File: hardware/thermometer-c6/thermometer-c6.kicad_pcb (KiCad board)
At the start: 2 copper layers, 49 x 36 mm, 101 parts, among them J1 JST-PH-2 BAT, J2 MEAS_HDR, J3 USB-C, J4 EPD FPC24 0.5mm, J5 DEBUG, Q1 AO3401A, Q2 AO3401A, Q3 Si1308EDL, Q4 AO3401A, Q5 2N7002, Q6 AO3401A, SW1 RESET, SW2 BOOT, U1 ESP32-C6-MINI-1-N4, U2 RT9080-33GJ5, U3 USBLC6-2SC6, U4 MCP73831-2, U5 BMP581, U6 BMP585, Y1 32.768kHz FC-135

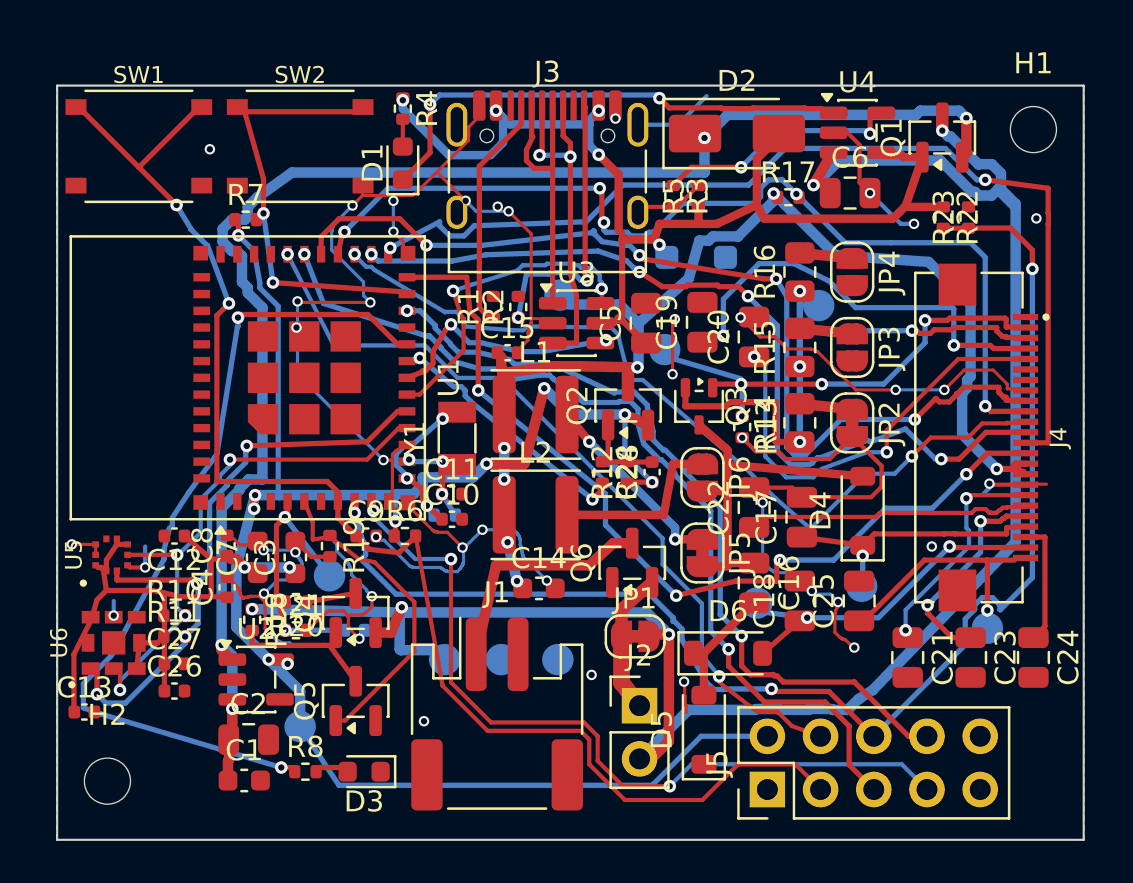
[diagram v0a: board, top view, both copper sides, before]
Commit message: Reclaim 48x35 board size; harvest user's GND re-stitch (0 unconnected)
Shrank BOARD to 48x35 (both east+south strips reclaimed to original
size). The outline shrink re-fragmented the GND pour into 3 opens
(C12.2, U3.2, an F<->B split); the user hand-closed them in the GUI.
Harvested wholesale (56 GND tracks / 44 stitch vias). Also adds
verify/gnd_islands.py -- a GND connectivity/robustness debugger
(island-aware via pcbnew GetUnconnectedCount; finds articulation vias +
recommends redundant-via spots). Gate: unconnected 0, REAL=0 (2 GND
dangling stubs deferred), check_pcb OK, make check green. Archive
snapshot of the solved board included.

Note: GND is connected but LOW-redundancy -- two sub-planes (~49/~38
pads) each hang off a single 0.15mm neck; hardening next.

Co-Authored-By: Claude Fable 5 <noreply@anthropic.com>
Claude-Session: https://claude.ai/code/session_017pkZ81qmZpNwwW2CABSh5y
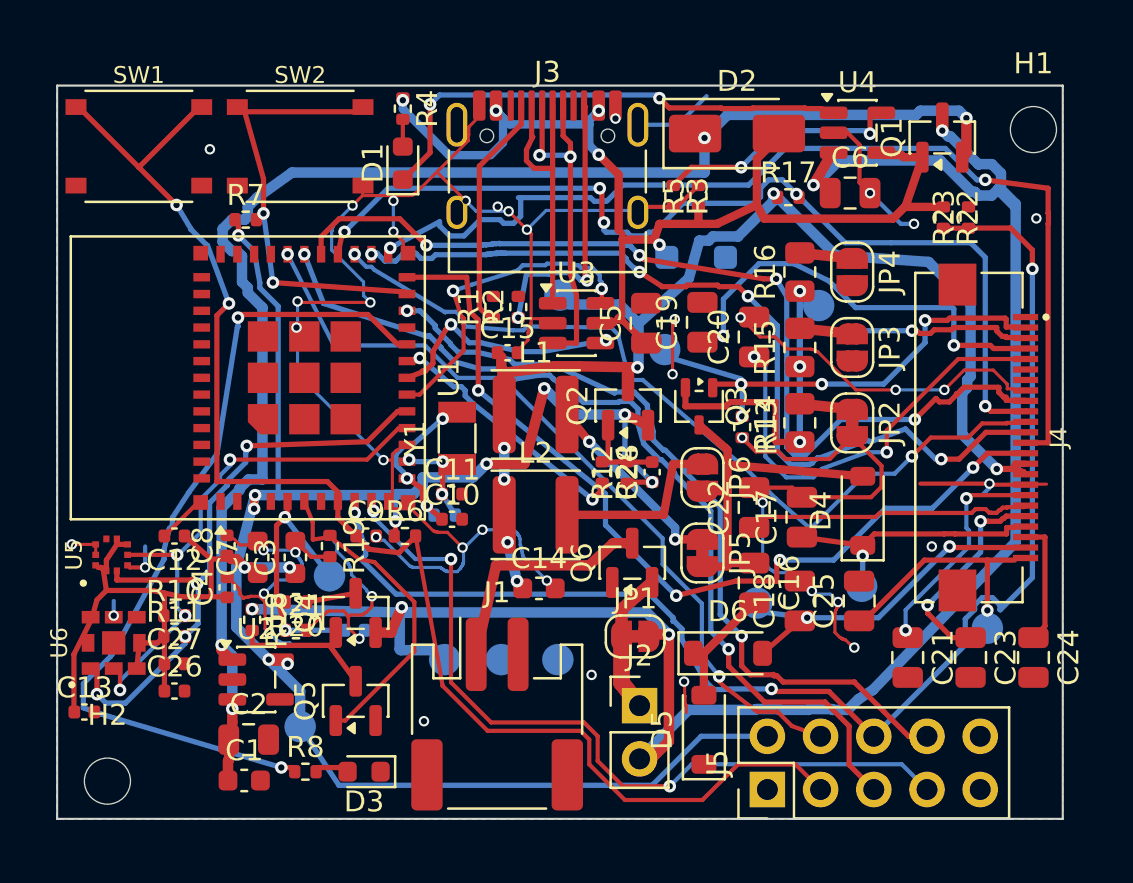
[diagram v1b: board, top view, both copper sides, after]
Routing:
- net GND: track 149.3 -> 161.5 mm, vias 43 -> 44
- net EPD_CS: track 40.5 -> 41.9 mm
- net EPD_SCK: track 47.6 -> 48.6 mm
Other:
- board size 49 x 36 mm -> 48 x 35 mm

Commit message: Harden GND: +10 redundant stitch vias, single-via SPOFs 28 -> 18
verify/gnd_islands.py audit found GND connected but a low-redundancy
tree. Added 10 GND stitch vias (0.5/0.3): 7 doubling small single-via
ties + 3 doubling the largest via-SPOFs (the 46/27-pad planes and the
user's 27-pad HV via @22.42,6.88 now has a redundant tie @23.0,6.5).
Single-via ties 28->18; the four biggest are de-SPOF'd. Gate REAL=0,
unconnected 0, check_pcb OK, make check green.

KNOWN RESIDUAL (needs a GUI reroute, not stitchable): the whole GND is
two board-spanning halves (~39 + ~61 pads) joined by ONE 0.15mm F.Cu
neck at the crystal/EN moat (TRACKS ~line 206) -- no bypass via exists
(the halves meet cross-layer only there) and widening fails DRC on the
crystal clearance. Opening a 2nd GND crossing of that moat is the top
robustness item.

Co-Authored-By: Claude Fable 5 <noreply@anthropic.com>
Claude-Session: https://claude.ai/code/session_017pkZ81qmZpNwwW2CABSh5y
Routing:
- net GND: vias 44 -> 54
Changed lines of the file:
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@@
+	)
+	(via
+		(at 100.85 122.74)
+		(size 0.5)
+		(drill 0.3)
+		(layers "F.Cu" "B.Cu")
+		(net "GND")
 	)
 	(via
@@
 	)
 	(via
+		(at 112.08 112.1)
+		(size 0.5)
+		(drill 0.3)
+		(layers "F.Cu" "B.Cu")
+		(net "GND")
+	)
+	(via
+		(at 113.3 105.43)
+		(size 0.5)
+		(drill 0.3)
+		(layers "F.Cu" "B.Cu")
+		(net "GND")
+	)
+	(via
 		(at 113.717 106.983)
 		(size 0.6)
@@
 	)
 	(via
+		(at 114.9 118.5)
+		(size 0.5)
+		(drill 0.3)
+		(layers "F.Cu" "B.Cu")
+		(net "GND")
+	)
+	(via
 		(at 114.95 110.35)
 		(size 0.5)
@@
 	)
 	(via
+		(at 117.06 105.79)
+		(size 0.5)
+		(drill 0.3)
+		(layers "F.Cu" "B.Cu")
+		(net "GND")
+	)
+	(via
 		(at 117.312 113.003)
 		(size 0.6)
@@
 	)
 	(via
+		(at 118.36 130.34)
+		(size 0.5)
+		(drill 0.3)
+		(layers "F.Cu" "B.Cu")
+		(net "GND")
+	)
+	(via
 		(at 118.37 119.5)
 		(size 0.6)
@@
 	)
 	(via
+		(at 123 106.5)
+		(size 0.5)
+		(drill 0.3)
+		(layers "F.Cu" "B.Cu")
+		(net "GND")
+	)
+	(via
 		(at 123.025 103.325)
 		(size 0.6)
@@
 	)
 	(via
+		(at 125.77 128.94)
+		(size 0.5)
+		(drill 0.3)
+		(layers "F.Cu" "B.Cu")
+		(net "GND")
+	)
+	(via
 		(at 125.85 101.2)
 		(size 0.6)
@@
 	)
 	(via
+		(at 126 123.3)
+		(size 0.5)
+		(drill 0.3)
+		(layers "F.Cu" "B.Cu")
+		(net "GND")
+	)
+	(via
 		(at 126.1 106.534)
 		(size 0.6)
@@
 	)
 	(via
+		(at 139.65 105.13)
+		(size 0.5)
+		(drill 0.3)
+		(layers "F.Cu" "B.Cu")
+		(net "GND")
+	)
+	(via

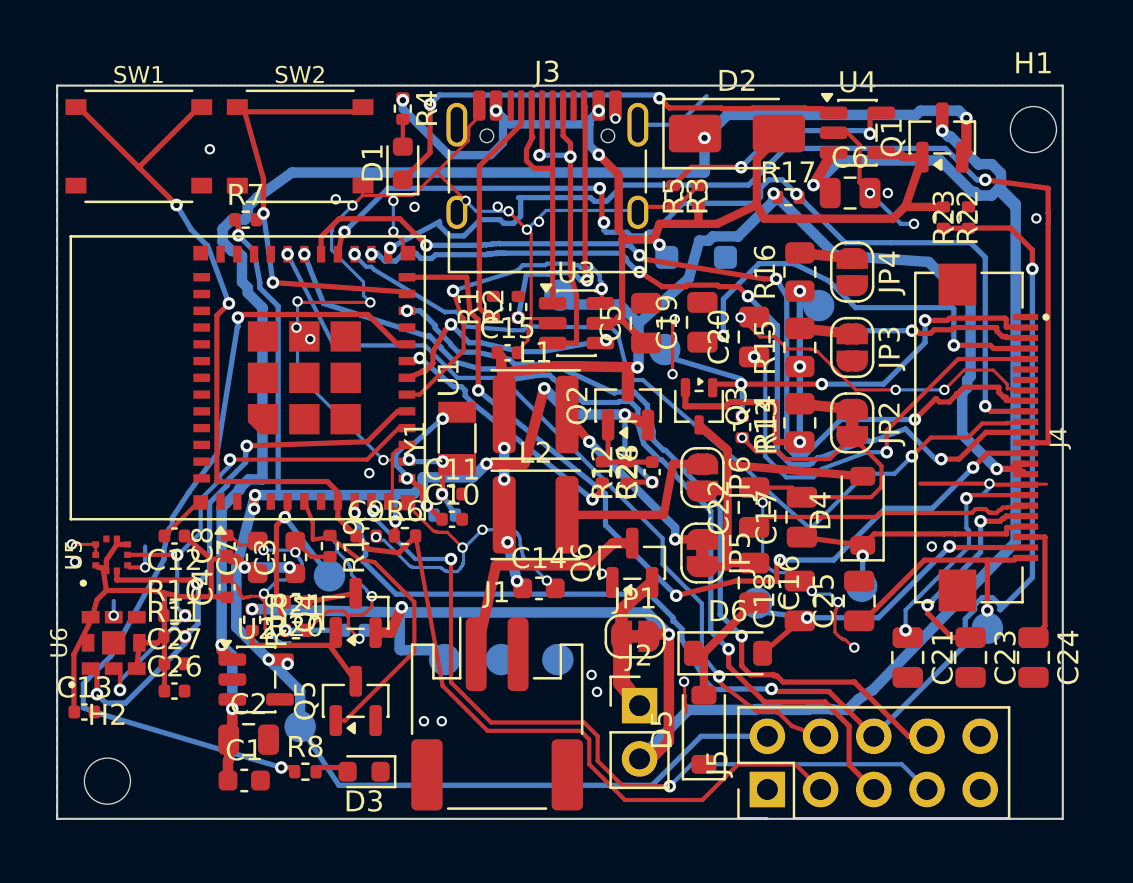
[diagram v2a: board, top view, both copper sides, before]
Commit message: Harvest GND-SPOF fixes + straighten all paths to fixpoint
Harvested the user's GND-robustness GUI pass (single-via SPOF ties
15->2, crystal/EN moat eliminated). Fixed the 2 hole_to_hole (nudged
GND stitch vias to >=0.25 hole-to-hole) + 2 dangling stubs their vias
introduced. Straightened both signal (pcb_routes) and GND (pcb_layout
TRACKS) polylines to a true fixpoint (re-run fresh until 0 accepted, 2
runs each): -138 vertices, -17.3mm copper -> more pour area.

straighten.py: added --layout (straighten pcb_layout GND TRACKS, STITCH
vias as junction guards) and FIXED a latent gate bug -- it waived
GND-unconnected, which on a finished board silently deleted a vertex on
U5.8's sensor-GND pad (under the fills=False keep-out, no pour fallback)
and disconnected it. Gate now requires unconnected==0 for all nets.

Gate REAL=0, unconnected 0, check_pcb OK, make check green, GND
connected. Archive snapshot of the user's solve included. Widen pass
next; not reviewed yet.

Co-Authored-By: Claude Fable 5 <noreply@anthropic.com>
Claude-Session: https://claude.ai/code/session_017pkZ81qmZpNwwW2CABSh5y
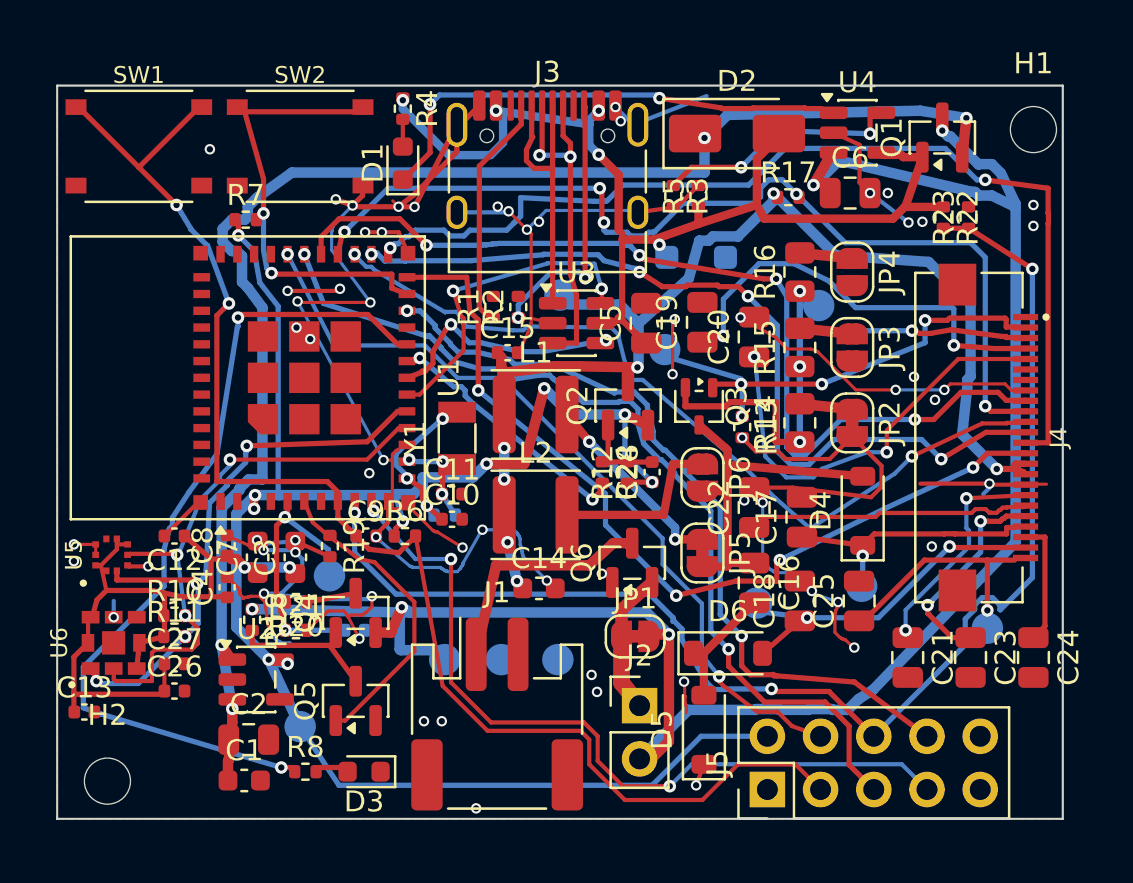
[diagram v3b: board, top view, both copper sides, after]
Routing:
- net GND: track 161.5 -> 176.6 mm, vias 54 -> 66
- net +3V3: track 112.4 -> 116.2 mm
- net SDA: track 25.6 -> 27.7 mm, vias 4 -> 3
- net EPD_CS: track 41.9 -> 40.2 mm
- net VBAT: track 91.5 -> 90.3 mm
- net SCL: track 29.9 -> 28.8 mm
- net EPD_MOSI: track 42.3 -> 41.5 mm
- net VBUS_SENSE: track 64.2 -> 63.5 mm
- net VBUS: track 53.1 -> 52.4 mm
- net EPD_DC: track 40.1 -> 39.5 mm
- net VDIV_EN: track 15.4 -> 14.8 mm
- net VSYS: track 72.2 -> 71.7 mm
- net Net-(J3-CC2): track 13.6 -> 13.1 mm

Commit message: Harvest hand-routed neck + east-cap GND SPOF fixes
North F.Cu GND neck (0.25mm, was sole tie for ~34 pads) re-laced; east-cap 16-pad SPOF given a 2nd tie via a 0.6/0.3 stitch at (44.70,6.40). Signals harvested via extract_tracks --all; GND vias -> STITCH (66->68, grown sizes preserved), lacing -> TRACKS. out/hand == generated is copper-identical (1075 segments / 191 vias, +0/-0 per net); DRC REAL=0, unconnected=0, starved=0; make check green.

Co-Authored-By: Claude Opus 4.8 (1M context) <noreply@anthropic.com>
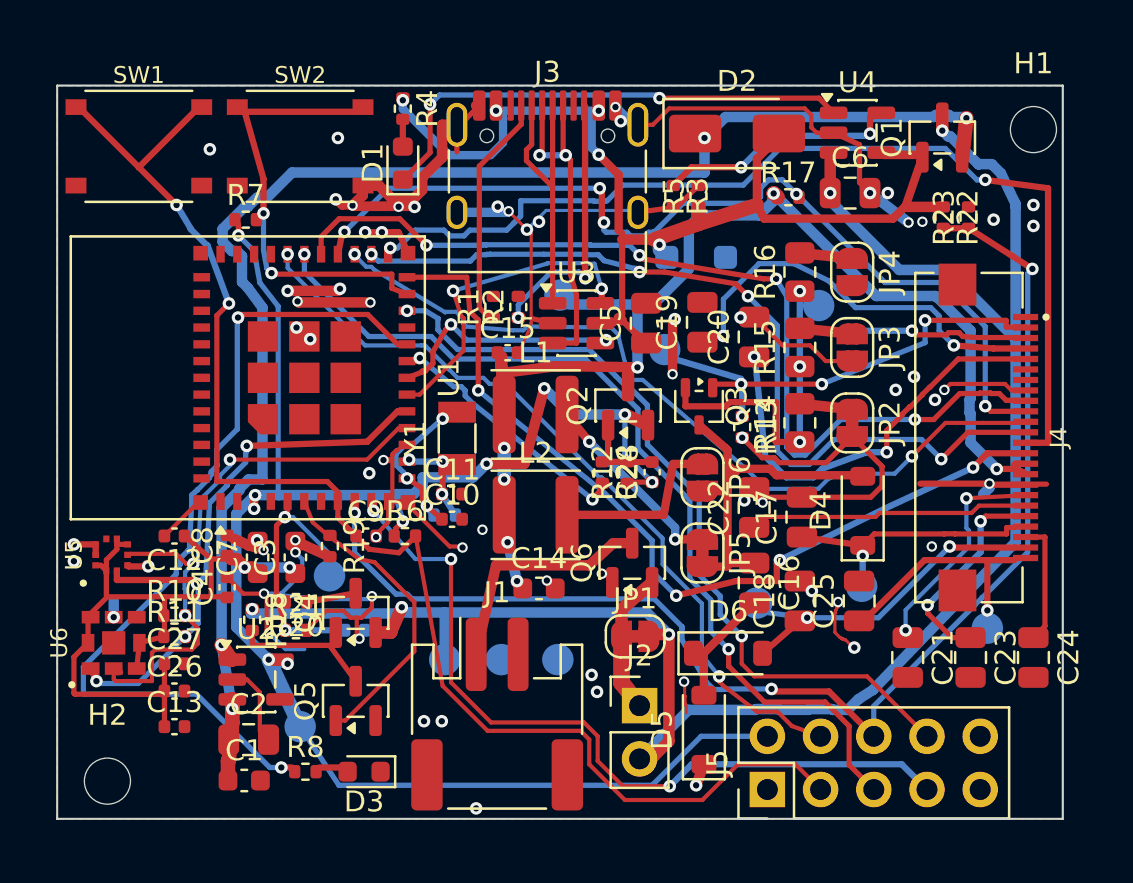
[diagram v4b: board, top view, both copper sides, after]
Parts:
- moved C12 9.44 mm to (105.6, 121.5), turned to 180 degrees
- moved C27 6.10 mm to (105.6, 127.6), turned to 0 degrees
- moved C13 1.70 mm to (105.6, 130.6)
- moved C26 1.30 mm to (105.6, 128.9)
- renumbered C13 to C12, C26 to C13, C27 to C26, C12 to C27
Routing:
- net GND: track 176.6 -> 150.6 mm, vias 66 -> 68
- net EPD_RST: track 46.8 -> 44.9 mm
- net VBUS_SENSE: track 63.5 -> 61.9 mm
- net LED_STATUS: track 40.2 -> 41.2 mm
- net DBG_IO8: track 37.4 -> 38.4 mm
- net SDA: track 27.7 -> 28.6 mm
- net +3V3: track 116.2 -> 117.0 mm
- net CHG_STAT: track 22.7 -> 23.5 mm
- net EPD_DC: track 39.5 -> 38.8 mm
- net Net-(J4-Pin_4): track 19.3 -> 18.7 mm
- net VBAT: track 90.3 -> 90.8 mm

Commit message: Straighten to fixpoint + widen traces/GND toward class caps
Straighten: signals -43 verts/-6.80mm, GND lacing -15 verts/-1.41mm (collapsed +3V3 B.Cu S-bend, DBG_RX slivers, EPD_CS/BUSY/USB_D kinks; VDIV_EN staircase is genuine corners, left). Widen: +8.1mm2 -- signals normalized toward 0.30, power/burst toward 0.70; GND neck (20.15,0.95) hardened 0.25->0.50. Converged in 2 straighten<->widen rounds. 0 vias pruned: NE double-stitch pair is mutually load-bearing, board is not over-stitched. DRC REAL=0/unconnected=0/starved=0, gnd_islands 1 island (no new SPOF), make check green, byte-stable.

Co-Authored-By: Claude Opus 4.8 (1M context) <noreply@anthropic.com>
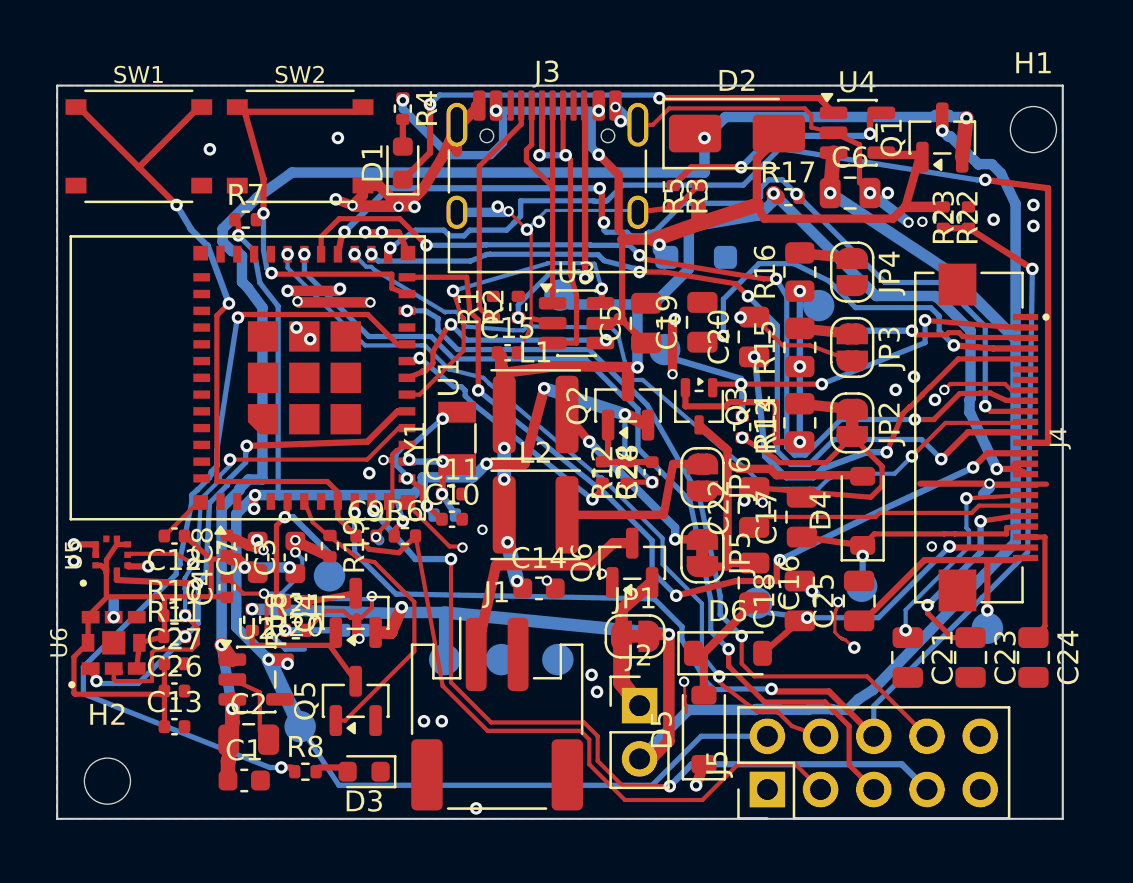
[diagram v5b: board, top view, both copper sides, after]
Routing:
- net GND: track 150.6 -> 149.2 mm
- net VBAT: track 90.8 -> 89.4 mm
- net LED_STATUS: track 41.2 -> 39.9 mm
- net DBG_IO8: track 38.4 -> 37.7 mm
- net EPD_SCK: track 48.1 -> 47.5 mm

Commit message: Harvest hand reroute pass; restore DBG_TX bridge dropped as graphic line
Large GUI simplification pass (~30 nets tidied: LED_STATUS -11, DBG_TX -10, VSYS/VBAT -8/-7, SDA/SCL -7/-5, USB_D+ -5, EPD_MOSI +4; vias unchanged). The DBG_TX gap had been bridged with a copper PCB_SHAPE graphic line, which extract_tracks (GetTracks only) drops -> reproduced as a proper netted DBG_TX track (0 unconnected, DRC-validated). Trimmed a 0.099mm EPD_DC dangling stub. Signals via extract_tracks --all; GND STITCH 68 (grown sizes preserved) + TRACKS 47. out/hand == generated (topo 59/59); DRC REAL=0, unconnected=0, starved=0; make check green; byte-stable. 27-pad B.Cu neck (#35) still open.

Co-Authored-By: Claude Opus 4.8 (1M context) <noreply@anthropic.com>
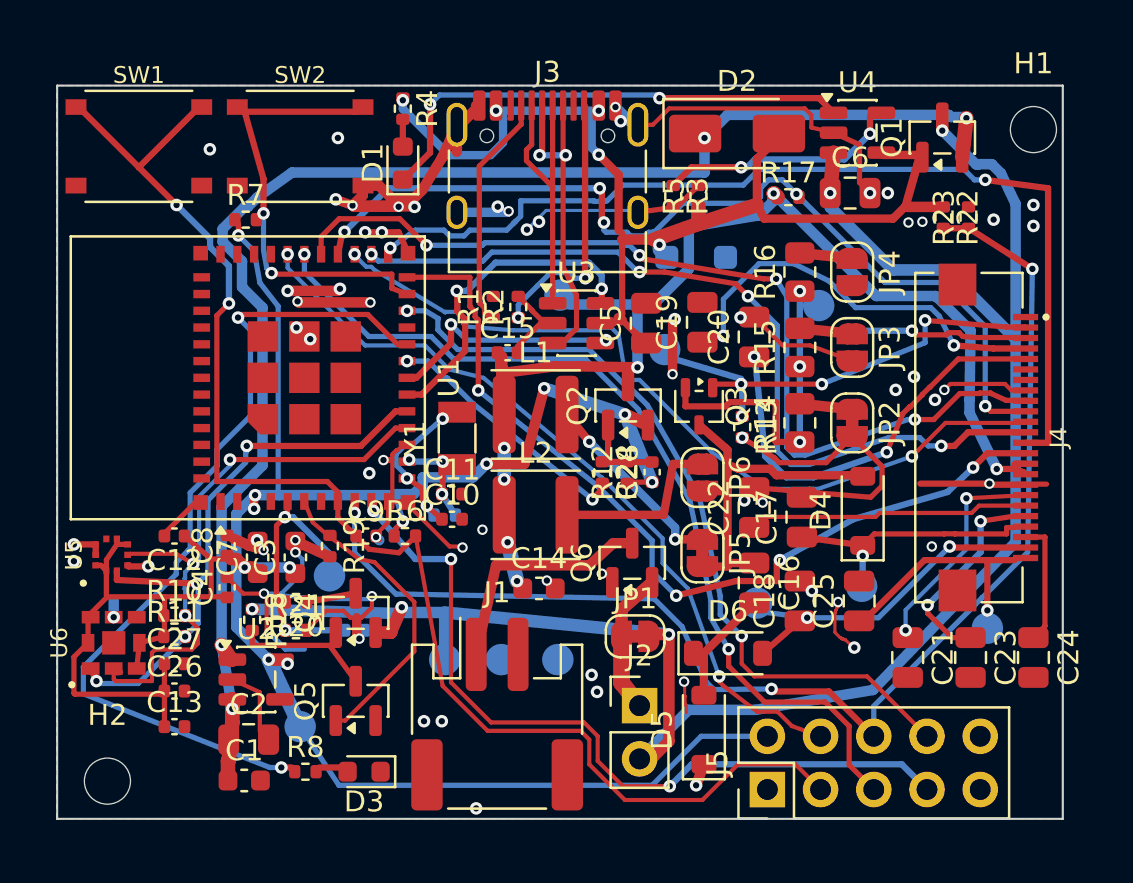
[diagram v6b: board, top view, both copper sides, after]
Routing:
- net GND: track 149.2 -> 142.7 mm
- net LED_STATUS: track 39.9 -> 40.8 mm
- net DBG_RX: track 43.7 -> 43.2 mm
- net EPD_CS: track 40.3 -> 39.8 mm
